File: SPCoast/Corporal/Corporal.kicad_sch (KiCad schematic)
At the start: 37 parts, among them SW829 829, SW831 831, SW900 829D, SW901 1

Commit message: fix(kicad): remaining class I circuits take the 0<n>T form
Owner-approved numbers: Luchessa 2SAT -> 02T; Christopher IND -> 01T;
Corporal IND -> 01T; GilroyInterchange Interchange -> 01T and TK1 -> 02T
(passing-track main and siding merged into class I). Desk lamp 1TK on
GilroyInterchange column 4 becomes 02T.

Verified: netlists rebuilt for the five projects; every 0<n>T is unique within
its plant; desk circuit tokens that match no plant circuit are down to four
(CP_Watsonville:SA1, CP_Watsonville:837T1, Watsonville 1NAK and 2NAK).

Co-Authored-By: Claude Sonnet 5.5 <noreply@anthropic.com>
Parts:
- TC5: value IND -> 01T
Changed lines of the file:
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@@
 			)
 		)
-		(property "Value" "IND"
+		(property "Value" "01T"
 			(at 145.29 65.79 0)
 			(show_name no)

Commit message: SPCoast: owner's edit: END_CTC corrected in library; Corporal B3 and Sargent B2 use IRJ-END_CTC (baseline)
Co-Authored-By: Claude Sonnet 5.5 <noreply@anthropic.com>
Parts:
- removed B3: (no value), symbol Railroad:IRJ
- added B3: END CTC, symbol Railroad:IRJ-END_CTC
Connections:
- net at B4.2 (B), DOT6.1 (To), TC5.1 (MC): now also B3.1 (CTC)
- net at SW901.1 (C): now also B3.2 (DARK)
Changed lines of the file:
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@@
+	)
+	(symbol
+		(lib_id "Railroad:IRJ-END_CTC")
+		(at 157.48 68.58 180)
+		(unit 1)
+		(body_style 1)
+		(exclude_from_sim no)
+		(in_bom yes)
+		(on_board yes)
+		(in_pos_files yes)
+		(dnp no)
+		(fields_autoplaced yes)
+		(property "Reference" "B3"
+			(at 157.48 61.595 0)
+			(hide yes)
+			(show_name no)
+			(do_not_autoplace no)
+			(effects
+				(font
+					(size 1.27 1.27)
+				)
+			)
+		)
+		(property "Value" "END CTC"
+			(at 157.1625 62.23 0)
+			(show_name no)
+			(do_not_autoplace no)
+			(effects
+				(font
+					(size 1.27 1.27)
+				)
+			)
+		)
+		(property "Footprint" ""
+			(at 157.48 68.58 0)
+			(hide yes)
+			(show_name no)
+			(do_not_autoplace no)
+			(effects
+				(font
+					(size 1.27 1.27)
+				)
+			)
+		)
+		(property "Datasheet" ""
+			(at 157.48 68.58 0)
+			(hide yes)
+			(show_name no)
+			(do_not_autoplace no)
+			(effects
+				(font
+					(size 1.27 1.27)
+				)
+			)
+		)
+		(property "Description" ""
+			(at 157.48 68.58 0)
+			(hide yes)
+			(show_name no)
+			(do_not_autoplace no)
+			(effects
+				(font
+					(size 1.27 1.27)
+				)
+			)
+		)
+		(property "Kind" "END_CTC"
+			(at 157.48 57.785 0)
+			(hide yes)
+			(show_name no)
+			(do_not_autoplace no)
+			(effects
+				(font
+					(size 1.27 1.27)
+				)
+			)
+		)
+		(property "Role" "TRACK"
+			(at 157.48 59.69 0)
+			(hide yes)
+			(show_name no)
+			(do_not_autoplace no)
+			(effects
+				(font
+					(size 1.27 1.27)
+				)
+			)
+		)
+		(pin "2"
+		)
+		(pin "1"
+		)
+		(instances
+			(project "Corporal"
+				(path "/ee580a7d-3bcc-4815-828e-1449721b556e"
+					(reference "B3")
+					(unit 1)
+				)
+			)
+		)
 	)
 	(symbol
@@
 					(unit 1)
 				)
-			)
-		)
-	)
-	(symbol
-		(lib_id "Railroad:IRJ")
-		(at 157.48 68.58 0)
-		(unit 1)
-		(body_style 1)
-		(exclude_from_sim no)
-		(in_bom yes)
-		(on_board yes)
-		(in_pos_files yes)
-		(dnp no)
-		(fields_autoplaced yes)
-		(property "Reference" "B3"
-			(at 157.48 71.12 0)
-			(hide yes)
-			(show_name no)
-			(do_not_autoplace no)
-			(effects
-				(font
-					(size 1.27 1.27)
-				)
-			)
-		)
-		(property "Value" ""
-			(at 157.48 68.58 0)
-			(hide yes)
-			(show_name no)
-			(do_not_autoplace no)
-			(effects
-				(font
-					(size 1.27 1.27)
-				)
-			)
-		)
-		(property "Footprint" ""
-			(at 157.48 68.58 0)
-			(hide yes)
-			(show_name no)
-			(do_not_autoplace no)
-			(effects
-				(font
-					(size 1.27 1.27)
-				)
-			)
-		)
-		(property "Datasheet" ""
-			(at 157.48 68.58 0)
-			(hide yes)
-			(show_name no)
-			(do_not_autoplace no)
-			(effects
-				(font
-					(size 1.27 1.27)
-				)
-			)
-		)
-		(property "Description" "Insulated Rail Joint"
-			(at 157.48 68.58 0)
-			(hide yes)
-			(show_name no)
-			(do_not_autoplace no)
-			(effects
-				(font
-					(size 1.27 1.27)
-				)
-			)
-		)
-		(property "Role" "TRACK"
-			(at 157.48 68.58 0)
-			(hide yes)
-			(show_name no)
-			(do_not_autoplace no)
-			(effects
-				(font
-					(size 1.27 1.27)
-				)
-			)
-		)
-		(property "Kind" "IRJ"
-			(at 157.48 68.58 0)
-			(hide yes)
-			(show_name no)
-			(do_not_autoplace no)
-			(effects
-				(font
-					(size 1.27 1.27)
-				)
-			)
-		)
-		(pin "2"
-		)
-		(pin "1"
-		)
-		(instances
-			(project "Corporal"
-				(path "/ee580a7d-3bcc-4815-828e-1449721b556e"
-					(reference "B3")
-					(unit 1)
-				)

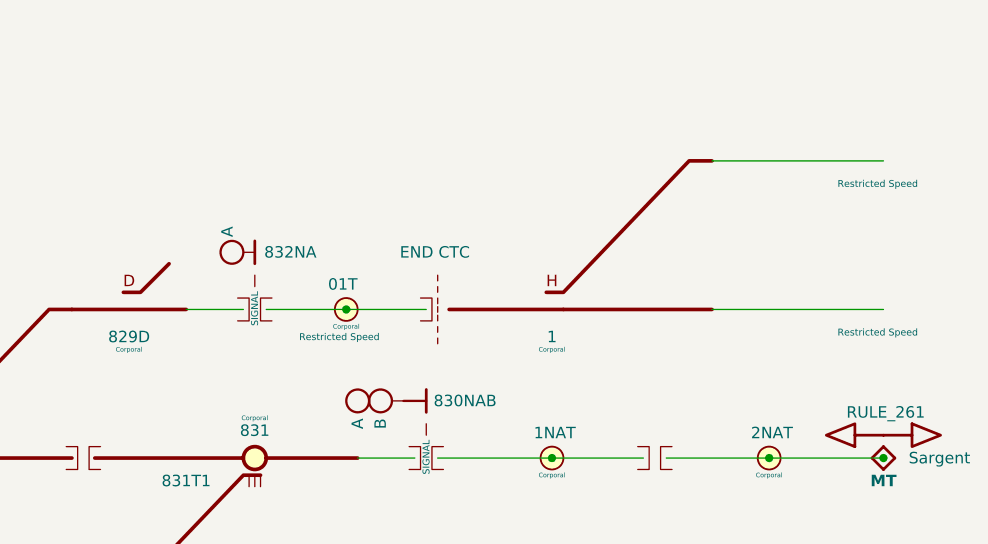
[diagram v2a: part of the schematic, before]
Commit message: SPCoast: owner's edits: schematics synced with the revised symbol libraries (baseline)
Update Symbols from Library on all plant and desk sheets; CP values for
Christopher, GilroyInterchange and Luchessa; Restricted Speed markers
consolidated in Corporal, Luchessa and Sargent.

Observed in the diff, not changed by the sweep that follows: CP changed on 23
symbols (Christopher: prefix removed, 815/815A/IND now Christopher North) and
added on 12 (GilroyInterchange); two lamps' Color reset to their symbol variant
(Christopher LMP93 red -> yellow, Sargent LMP133 yellow -> red).

Verified: netlists keep their net counts (Christopher 33, Corporal 26,
GilroyCalTrain 27, GilroyInterchange 22, Luchessa 34, Sargent 18, Watsonville
96, South-cTc 341); desk compiles to 75 appliances, 137 bindings, 14 columns;
no root-UUID regression.

Co-Authored-By: Claude Sonnet 5.5 <noreply@anthropic.com>
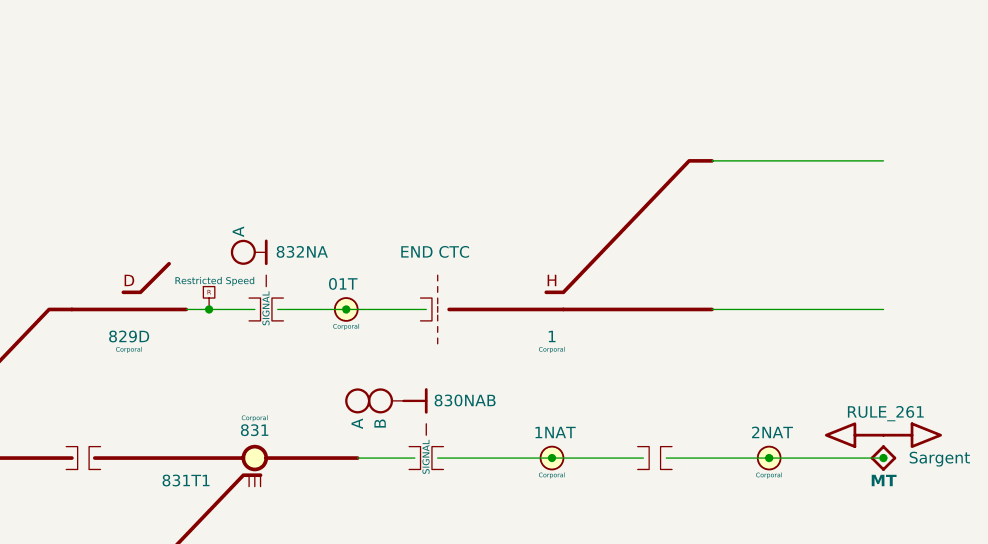
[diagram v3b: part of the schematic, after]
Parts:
- removed DOT1, DOT5: Restricted Speed, symbol Railroad:Rule105-RestrictedSpeed
- DOT6: Name Movement on Other Than Main Track -> (none)
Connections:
- net at B4.1 (A), SW900.2 (R): now also DOT6.1 (To)
- net at B3.1 (CTC), B4.2 (B), TC5.1 (TC): no longer DOT6.1 (To)

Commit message: chore(kicad): sweep instance Role/Kind and stale fields to the library vocabulary
Scripted, one pass over every sheet except Watsonville (open in KiCad, locked):
- Role/Kind of placed symbols refreshed from the library by lib_id: 10 Role
  (MAIN HOUSE CONTROLLED_POINT -> CONTROL_POINT, Rule251-DoT empty) and 17 Kind
  (IRJ-Signal IRJ -> IRJ_SIGNAL x7, Mast_Single/Double swaps, HandThrow
  -> SWITCH_MANUAL, Derail, PanelLock -> LOCK_LEVER, NextCP).
- Stale instance fields dropped where the library no longer has them: 39 Name,
  28 Direction (all empty or retired), 5 CP on Bumper and IRJ symbols.
- Orphan embedded copies of the retired symbol Rule6.28-OtherThanMain removed
  from two sheets (unused).

Not done: Watsonville (locked); CMRInet -> CMRI (library Kind still CMRInet);
fields new to the library (MAIN HOUSE Kind, switch Indications) are not copied
onto instances, the compiler will read library defaults by lib_id; Rulebook
fields stay until the compiler stops requiring them.

Verified: per-symbol before/after comparison shows only these changes, same
symbol sets, positions and lib_ids; netlists keep their net counts (Christopher
33, Corporal 26, GilroyCalTrain 27, GilroyInterchange 22, Luchessa 34, Sargent
18, South-cTc 341); desk still 75 appliances, 137 bindings, 14 columns.

Co-Authored-By: Claude Sonnet 5.5 <noreply@anthropic.com>
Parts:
- DOT2: Name Track Signaled in One Direction -> (none)
- HOUSE1: Role CONTROLLED_POINT -> CONTROL_POINT
- SW900: Kind SWITCH_POWERED -> DERAIL
- SW901: Kind SWITCH_POWERED -> SWITCH_MANUAL
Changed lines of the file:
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@@
 			)
 		)
-		(property "Kind" "SWITCH_POWERED"
+		(property "Kind" "DERAIL"
 			(at 123.19 68.58 0)
 			(hide yes)
@@
 			)
 		)
-		(property "Name" "Track Signaled in One Direction"
-			(at 64.135 78.105 0)
-			(hide yes)
-			(show_name no)
-			(do_not_autoplace no)
-			(effects
-				(font
-					(size 1.27 1.27)
-				)
-			)
-		)
 		(property "Role" "POLICY"
 			(at 63.5 82.55 0)
@@
 			)
 		)
-		(property "Kind" "SWITCH_POWERED"
+		(property "Kind" "SWITCH_MANUAL"
 			(at 170.18 68.58 0)
 			(hide yes)
@@
 			)
 		)
-		(property "Role" "CONTROLLED_POINT"
+		(property "Role" "CONTROL_POINT"
 			(at 99.06 41.91 0)
 			(hide yes)

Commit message: chore(kicad): masts and maintainer calls carry no CP; IRJ-Signals do; CMRInet Kind is CMRI
Owner decision: an IRJ-Signal is the single source of a signal's control point
(a mast attaches to exactly one IRJ-Signal through its SIGNAL pin); a
maintainer call is tied to its house by the netlist.
- CP dropped from 23 masts and 5 maintainer calls.
- 7 empty IRJ-Signal CPs filled with the plant's only house (Corporal, Sargent).
- 43 empty Name fields that KiCad re-added to Christopher dropped again.
- Codeline-Transport Kind CMRInet -> CMRI on the placed instance and the
  embedded library copy (South-cTc root sheet).

Verified: per-symbol before/after comparison shows only these changes; every
IRJ-Signal in all seven plants has a CP naming one of its plant's houses; net
counts unchanged (Christopher 33, Corporal 26, GilroyCalTrain 27,
GilroyInterchange 22, Luchessa 34, Sargent 18, Watsonville 96, South-cTc 341);
desk compiles to 75 appliances, 137 bindings, 14 columns. Remaining CP
diagnostic: Sargent's Corporal:2NAT placeholder (cross-plant reference).

Co-Authored-By: Claude Sonnet 5.5 <noreply@anthropic.com>
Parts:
- B1, B2, B4, B5: CP (none) -> Corporal
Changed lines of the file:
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@@
 			)
 		)
-		(property "CP" ""
+		(property "CP" "Corporal"
 			(at 136.525 66.675 0)
 			(show_name no)
@@
 			)
 		)
-		(property "CP" ""
+		(property "CP" "Corporal"
 			(at 83.185 103.505 0)
 			(show_name no)
@@
 			)
 		)
-		(property "CP" ""
+		(property "CP" "Corporal"
 			(at 154.305 83.185 0)
 			(show_name no)
@@
 			)
 		)
-		(property "CP" ""
+		(property "CP" "Corporal"
 			(at 83.185 86.995 0)
 			(show_name no)

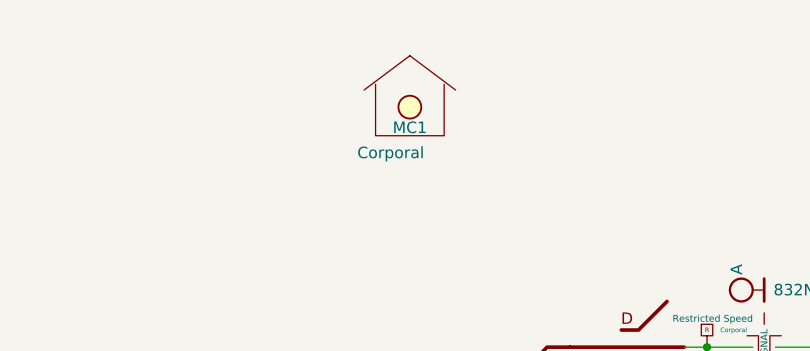
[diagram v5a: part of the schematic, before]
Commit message: SPCoast: owner's edits: Interlocking symbol on every Trackplan; MAIN HOUSE is STRUCTURE/CONTROL_POINT (baseline)
Each plant has one Interlocking symbol (Value is the authoritative name) and
every MAIN HOUSE's Interlocking pin is wired to it. Library Role/Kind:
Interlocking is STRUCTURE/INTERLOCKING, MAIN HOUSE is STRUCTURE/CONTROL_POINT
(refreshed on all instances by the owner).

Verified: one Interlocking symbol per plant; every house shares a net with it;
net counts are one higher than before in each plant (Christopher 34, Corporal
27, GilroyCalTrain 28, GilroyInterchange 23, Luchessa 35, Sargent 19,
Watsonville 97); no root-UUID regression; no symbol moved or removed.

Co-Authored-By: Claude Sonnet 5.5 <noreply@anthropic.com>
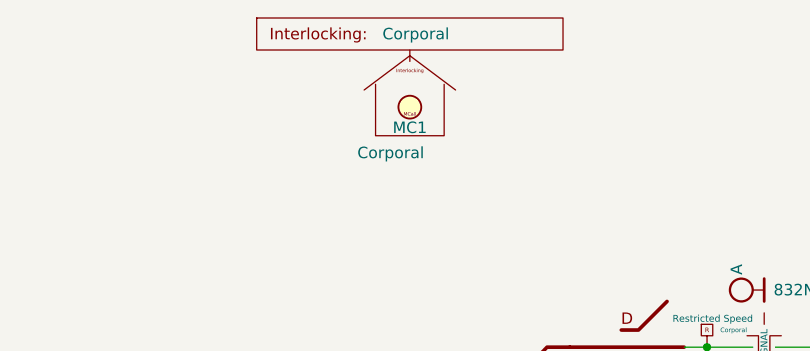
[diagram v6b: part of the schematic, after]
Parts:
- added Plant1: ${TITLE}, symbol Railroad:Interlocking
- HOUSE1: Kind (none) -> CONTROL_POINT; Milepost FIXME -> 83.0; Role CONTROL_POINT -> STRUCTURE
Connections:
- new net: HOUSE1.2 (Interlocking), Plant1.1 (Interlocking)
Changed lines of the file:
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@@
 			)
 		)
-		(property "Description" "Rrepresents the Control Point Maintainer Bungalow (plus optional Maintainer Call)"
+		(property "Description" "The Control Point Maintainer Bungalow (plus optional Maintainer Call)"
 			(at 99.06 47.625 0)
 			(hide yes)
@@
 			)
 		)
-		(property "Milepost" "FIXME"
-			(at 99.06 47.63 0)
-			(hide yes)
-			(show_name no)
-			(do_not_autoplace no)
-			(effects
-				(font
-					(size 1.27 1.27)
-				)
-			)
-		)
-		(property "Role" "CONTROL_POINT"
-			(at 99.06 41.91 0)
+		(property "Milepost" "83.0"
+			(at 99.06 47.625 0)
+			(hide yes)
+			(show_name no)
+			(do_not_autoplace no)
+			(effects
+				(font
+					(size 1.27 1.27)
+				)
+			)
+		)
+		(property "Role" "STRUCTURE"
+			(at 83.82 39.37 0)
+			(hide yes)
+			(show_name no)
+			(do_not_autoplace no)
+			(effects
+				(font
+					(size 1.27 1.27)
+				)
+			)
+		)
+		(property "Kind" "CONTROL_POINT"
+			(at 85.725 41.402 0)
 			(hide yes)
 			(show_name no)
@@
 		)
 		(pin "1"
+		)
+		(pin "2"
 		)
 		(instances
@@
 					(unit 1)
 				)
+			)
+		)
+	)
+	(symbol
+		(lib_id "Railroad:Interlocking")
+		(at 99.06 36.83 0)
+		(unit 1)
+		(body_style 1)
+		(exclude_from_sim no)
+		(in_bom yes)
+		(on_board yes)
+		(in_pos_files yes)
+		(dnp no)
+		(fields_autoplaced yes)
+		(property "Reference" "Plant1"
+			(at 84.836 30.988 0)
+			(hide yes)
+			(show_name no)
+			(do_not_autoplace no)
+			(effects
+				(font
+					(size 1.27 1.27)
+				)
+			)
+		)
+		(property "Value" "${TITLE}"
+			(at 96.012 33.782 0)
+			(show_name no)
+			(do_not_autoplace yes)
+			(effects
+				(font
+					(size 1.27 1.27)
+				)
+				(justify left)
+			)
+		)
+		(property "Footprint" ""
+			(at 99.06 36.83 0)
+			(hide yes)
+			(show_name no)
+			(do_not_autoplace no)
+			(effects
+				(font
+					(size 1.27 1.27)
+				)
+			)
+		)
+		(property "Datasheet" ""
+			(at 99.06 36.83 0)
+			(hide yes)
+			(show_name no)
+			(do_not_autoplace no)
+			(effects
+				(font
+					(size 1.27 1.27)
+				)
+			)
+		)
+		(property "Description" ""
+			(at 99.06 36.83 0)
+			(hide yes)
+			(show_name no)
+			(do_not_autoplace no)
+			(effects
+				(font
+					(size 1.27 1.27)
+				)
+			)
+		)
+		(property "Role" "STRUCTURE"
+			(at 87.757 27.178 0)
+			(hide yes)
+			(show_name no)
+			(do_not_autoplace no)
+			(effects
+				(font
+					(size 1.27 1.27)
+				)
+			)
+		)
+		(property "Kind" "INTERLOCKING"
+			(at 89.154 28.829 0)
+			(hide yes)
+			(show_name no)
+			(do_not_autoplace no)
+			(effects
+				(font
+					(size 1.27 1.27)
+				)
+			)
+		)
+		(pin "1"
+		)
+		(instances
+			(project "Corporal"
+				(path "/ee580a7d-3bcc-4815-828e-1449721b556e"
+					(reference "Plant1")
+					(unit 1)
+				)

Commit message: chore(kicad): refresh instances to the ADR 0003 libraries (InterlockingPlant 95f53e2)
- Desk sheets (South-cTc/*) and the Sargent sandbox: embedded PanelSwitch, PanelLock,
  PanelSignal, PanelMCall, PanelCode, PanelLamp-*, PanelColumn-MAX7313 definitions refreshed
  from the library (refresh_embedded.py, checked against the pre-pass library: only Description
  text had drifted). Instance Role APPLIANCE -> PANEL (77).
- Plant sheets: powered-switch instance Kind SWITCH_POWERED -> SWITCH_REMOTE (21), matching the
  library (sweep_role_kind_fields.py).

Verified:
- verify_symbol_diff.py: same symbols, lib_ids and positions; only Role/Kind changed.
- Nets unchanged: Christopher 30, Corporal 27, GilroyCalTrain 28, GilroyInterchange 23,
  Luchessa 35, Sargent 61, Watsonville 99, South-cTc 341.
- parse_kicad_plant.py --format text identical before/after for all seven plants.
- Desk compile 75/137/14, diagnostics identical; the 7 desk locks bind WLS/~{WLS}/~{WLK}/WLK
  to the bits that were NWS/RWS/RWK/NWK.
- No sheet or project outside Luchessa carries the copied root UUID.

Co-Authored-By: Claude Opus 5.5 <noreply@anthropic.com>
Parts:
- SW831: Kind SWITCH_POWERED -> SWITCH_REMOTE
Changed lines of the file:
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@@
 			)
 		)
-		(property "Kind" "SWITCH_POWERED"
+		(property "Kind" "SWITCH_REMOTE"
 			(at 137.16 85.09 0)
 			(hide yes)
